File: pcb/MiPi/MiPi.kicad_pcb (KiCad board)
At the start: 2 copper layers, 91 parts, among them J1 Micro_SD_Card, J2 AudioJack3, J3 USB_C_Receptacle_USB2.0_14P, Q1 Si1308EDL, SW1 SW_Push, SW2 SW_Push, SW3 RotaryEncoder_Switch_MP, SW4 SW_Push, SW5 SW_Push, SW6 SW_Push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

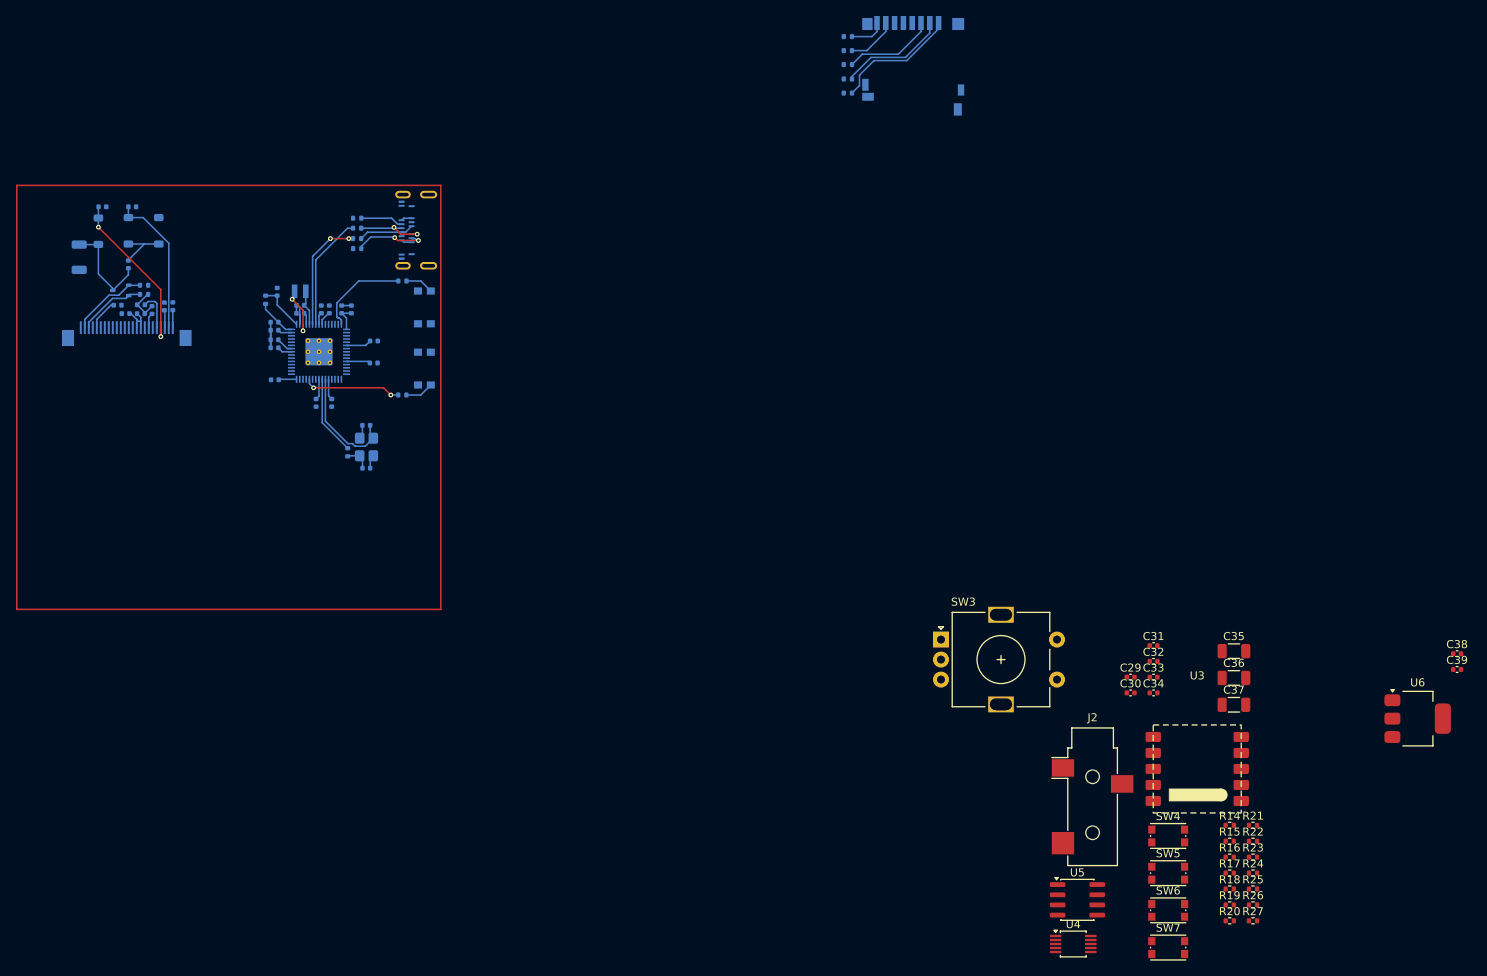
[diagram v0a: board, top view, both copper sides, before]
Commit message: Routed the analog switch and audio amp and audio jack
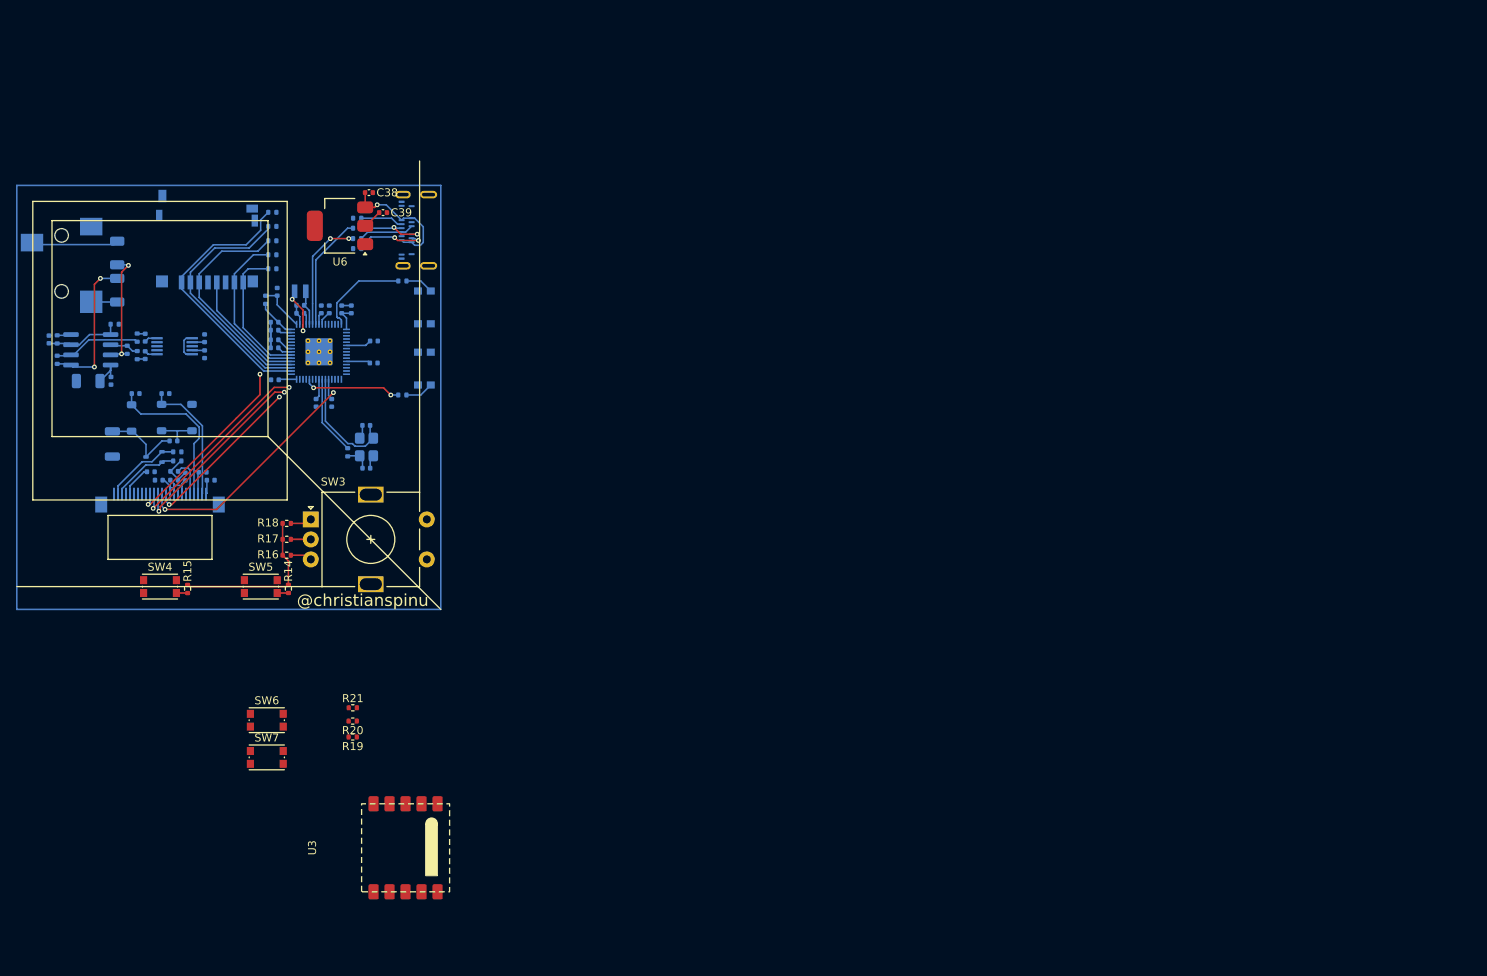
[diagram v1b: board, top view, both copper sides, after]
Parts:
- C29, C30, C31, C32, C33, C34, C35, C36, C37, J2, R22, R23, R24, R25, R26, R27, U4, U5: moved to B.Cu
- moved R27 166.2 mm to (80.0, 76.9), turned to 90 degrees
- moved R24 162.7 mm to (80.0, 79.5), turned to -90 degrees
- moved R26 159.7 mm to (87.1, 75.0), turned to 180 degrees
- moved R25 156.0 mm to (88.7, 78.2), turned to -90 degrees
- moved R22 153.0 mm to (89.9, 76.7), turned to 90 degrees
- moved R23 152.9 mm to (89.9, 78.9), turned to 90 degrees
- moved C37 150.6 mm to (87.5, 66.1), turned to 90 degrees
- moved U6 148.1 mm to (115.3, 62.7), turned to 180 degrees
- moved C36 147.8 mm to (87.5, 70.8), turned to -90 degrees
- moved C38 147.7 mm to (118.9, 58.5)
- moved C35 147.1 mm to (83.8, 82.1), turned to 180 degrees
- moved C39 145.9 mm to (120.7, 61.0)
- moved J2 145.6 mm to (80.5, 66.4), turned to 180 degrees
- moved C33 144.4 mm to (78.9, 76.9), turned to 90 degrees
- moved U5 141.2 mm to (84.2, 78.2)
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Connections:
- C38 pad 1: /REG_VIN -> +5V
- J1 pad 1: /peripherals/DAT2 -> /GP20
- J1 pad 2: /peripherals/DAT3 -> /GP21
- J1 pad 3: /peripherals/CMD -> /GP22
- J1 pad 5: /peripherals/SD_CLK -> /GP23
- J1 pad 7: /peripherals/DAT0 -> /GP24
- J1 pad 8: /peripherals/DAT1 -> /GP25
- R10 pad 1: /peripherals/DAT3 -> /GP21
- R11 pad 1: /peripherals/CMD -> /GP22
- R12 pad 1: /peripherals/DAT0 -> /GP24
- R13 pad 1: /peripherals/DAT1 -> /GP25
- R9 pad 1: /peripherals/DAT2 -> /GP20
- U1 pad 32: unconnected-(U1-GPIO20-Pad32) -> /GP20
- U1 pad 33: unconnected-(U1-GPIO21-Pad33) -> /GP21
- U1 pad 34: unconnected-(U1-GPIO22-Pad34) -> /GP22
- U1 pad 35: unconnected-(U1-GPIO23-Pad35) -> /GP23
- U1 pad 36: unconnected-(U1-GPIO24-Pad36) -> /GP24
- U1 pad 37: unconnected-(U1-GPIO25-Pad37) -> /GP25
- U6 pad 3: /REG_VIN -> +5V
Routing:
- net /GP20: track 0.00 -> 34.4 mm
- net /GP21: track 0.00 -> 31.4 mm
- net /peripherals/CLK: track 0.00 -> 29.2 mm, vias 0 -> 2
- net +3.3V: track 31.4 -> 59.7 mm
- net /GP22: track 0.00 -> 28.3 mm
- net /peripherals/D/C: track 0.00 -> 25.1 mm, vias 0 -> 2
- net /peripherals/CS: track 0.00 -> 24.3 mm, vias 0 -> 2
- net /peripherals/RES: track 0.00 -> 23.6 mm, vias 0 -> 2
- net /peripherals/SDI: track 0.00 -> 20.8 mm, vias 0 -> 2
- net /GP24: track 0.00 -> 20.4 mm
- net Net-(C36-Pad1): track 0.00 -> 18.4 mm, vias 0 -> 2
- net /GP25: track 0.00 -> 17.6 mm
- net /peripherals/DAT2: track 15.6 -> 0.00 mm
- net /GP23: track 0.00 -> 15.5 mm
- net Net-(C37-Pad1): track 0.00 -> 15.1 mm, vias 0 -> 2
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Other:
- board text added: "@christianspinu"

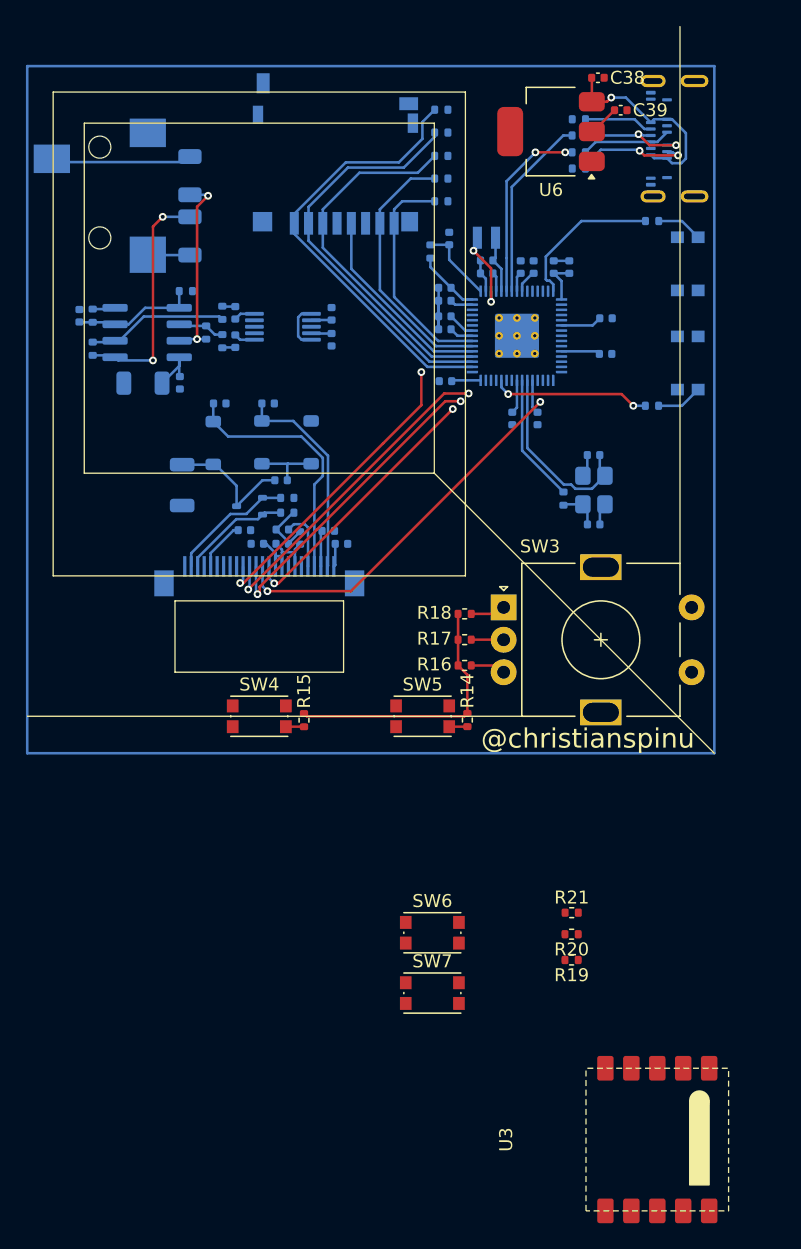
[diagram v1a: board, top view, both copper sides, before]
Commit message: Done the PCB layout
Remaining ground planes and power routing
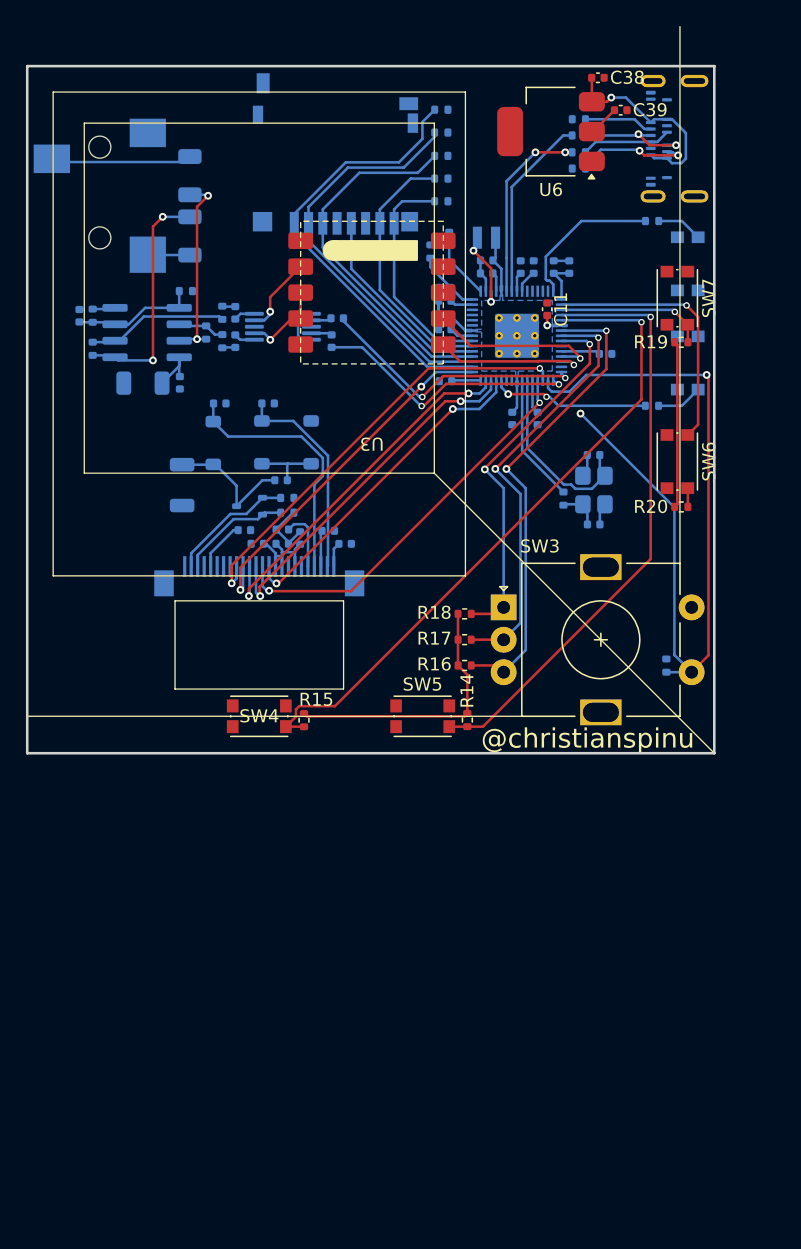
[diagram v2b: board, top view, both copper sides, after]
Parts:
- C11: moved to F.Cu
- R21: moved to B.Cu
- moved U3 68.9 mm to (101.5, 75.1), turned to 180 degrees
- moved SW7 56.8 mm to (125.0, 75.5), turned to -90 degrees
- moved R19 48.4 mm to (125.3, 79.0), turned to 0 degrees
- moved SW6 41.0 mm to (125.0, 88.2), turned to -90 degrees
- moved R20 34.0 mm to (125.3, 91.7), turned to 0 degrees
- moved R21 20.4 mm to (124.2, 103.9), turned to 90 degrees
- moved C11 4.59 mm to (115.0, 76.4), turned to 90 degrees
- moved C29 0.56 mm to (98.8, 77.1), turned to 180 degrees
- moved C25 0.28 mm to (99.4, 94.5)
- moved C30 0.11 mm to (98.4, 78.9)
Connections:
- C29 pad 1: /peripherals/PI_LOUT -> /GP11
- C30 pad 1: /peripherals/PI_ROUT -> /GP12
- R14 pad 1: /peripherals/SW4 -> /GP2
- R15 pad 1: /peripherals/SW3 -> /GP3
- R16 pad 1: /peripherals/RE_B -> /GP4
- R17 pad 1: /peripherals/RE_C -> /GP5
- R18 pad 1: /peripherals/RE_A -> /GP6
- R19 pad 2: /peripherals/SW1 -> /GP1
- R20 pad 2: /peripherals/SW2 -> /GP0
- R21 pad 1: /peripherals/RE_SW -> /GP13
- SW3 pad A: /peripherals/RE_A -> /GP6
- SW3 pad B: /peripherals/RE_B -> /GP4
- SW3 pad C: /peripherals/RE_C -> /GP5
- SW3 pad S1: /peripherals/RE_SW -> /GP13
- SW4 pad 2: /peripherals/SW3 -> /GP3
- SW5 pad 2: /peripherals/SW4 -> /GP2
- SW6 pad 1: /peripherals/SW2 -> /GP0
- SW7 pad 1: /peripherals/SW1 -> /GP1
- U1 pad 12: unconnected-(U1-GPIO8-Pad12) -> /GP8
- U1 pad 13: unconnected-(U1-GPIO9-Pad13) -> /GP9
- U1 pad 15: unconnected-(U1-GPIO11-Pad15) -> /GP11
- U1 pad 16: unconnected-(U1-GPIO12-Pad16) -> /GP12
- U1 pad 17: unconnected-(U1-GPIO13-Pad17) -> /GP13
- U1 pad 18: unconnected-(U1-GPIO14-Pad18) -> /GP14
- U1 pad 19: unconnected-(U1-GPIO15-Pad19) -> /GP15
- U1 pad 2: unconnected-(U1-GPIO0-Pad2) -> /GP0
- U1 pad 27: unconnected-(U1-GPIO16-Pad27) -> /GP16
- U1 pad 28: unconnected-(U1-GPIO17-Pad28) -> /GP17
- U1 pad 29: unconnected-(U1-GPIO18-Pad29) -> /GP18
- U1 pad 3: unconnected-(U1-GPIO1-Pad3) -> /GP1
- U1 pad 31: unconnected-(U1-GPIO19-Pad31) -> /GP19
- U1 pad 4: unconnected-(U1-GPIO2-Pad4) -> /GP2
- U1 pad 5: unconnected-(U1-GPIO3-Pad5) -> /GP3
- U1 pad 7: unconnected-(U1-GPIO4-Pad7) -> /GP4
- U1 pad 8: unconnected-(U1-GPIO5-Pad8) -> /GP5
- U1 pad 9: unconnected-(U1-GPIO6-Pad9) -> /GP6
- U2 pad 10: /peripherals/RES -> /GP19
- U2 pad 11: /peripherals/D/C -> /GP18
- U2 pad 12: /peripherals/CS -> /GP17
- U2 pad 13: /peripherals/CLK -> /GP15
- U2 pad 14: /peripherals/SDI -> /GP16
- U2 pad 9: /peripherals/BUSY -> /GP14
- U3 pad 1: /peripherals/FM_SDA -> /GP9
- U3 pad 2: /peripherals/FM_SCL -> /GP8
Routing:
- net /GP13: track 0.00 -> 62.5 mm, vias 0 -> 2
- net /GP3: track 0.00 -> 51.8 mm, vias 0 -> 1
- net /GP2: track 0.00 -> 46.5 mm, vias 0 -> 1
- net /GP4: track 0.00 -> 37.0 mm, vias 0 -> 2
- net /GP14: track 0.00 -> 34.1 mm, vias 0 -> 2
- net /GP5: track 0.00 -> 33.4 mm, vias 0 -> 2
- net /GP15: track 0.00 -> 30.9 mm, vias 0 -> 2
- net /GP6: track 0.00 -> 29.3 mm, vias 0 -> 2
- net /peripherals/CLK: track 29.2 -> 0.00 mm, vias 2 -> 0
- net /GP18: track 0.00 -> 28.1 mm, vias 0 -> 2
- net /GP19: track 0.00 -> 27.9 mm, vias 0 -> 2
- net /GP17: track 0.00 -> 27.8 mm, vias 0 -> 2
- net /GP16: track 0.00 -> 25.6 mm, vias 0 -> 2
- net /peripherals/D/C: track 25.1 -> 0.00 mm, vias 2 -> 0
- net /peripherals/CS: track 24.3 -> 0.00 mm, vias 2 -> 0
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- added copper zone on B.Cu, net +1V1
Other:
- board outline added: 53 x 53 mm
